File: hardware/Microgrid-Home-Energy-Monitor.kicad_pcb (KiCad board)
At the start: 2 copper layers, 41 parts, among them J1 AudioJack2, J2 AudioJack2, J3 Conn_01x04, J4 USB_C_Receptacle_USB2.0_16P, J5 Conn_01x06, J6 Conn_01x03, SW1 SW_Push, SW2 SW_Push, U1 ESP32-WROOM-32, U2 MCP6002-xP, U3 AMS1117-3.3

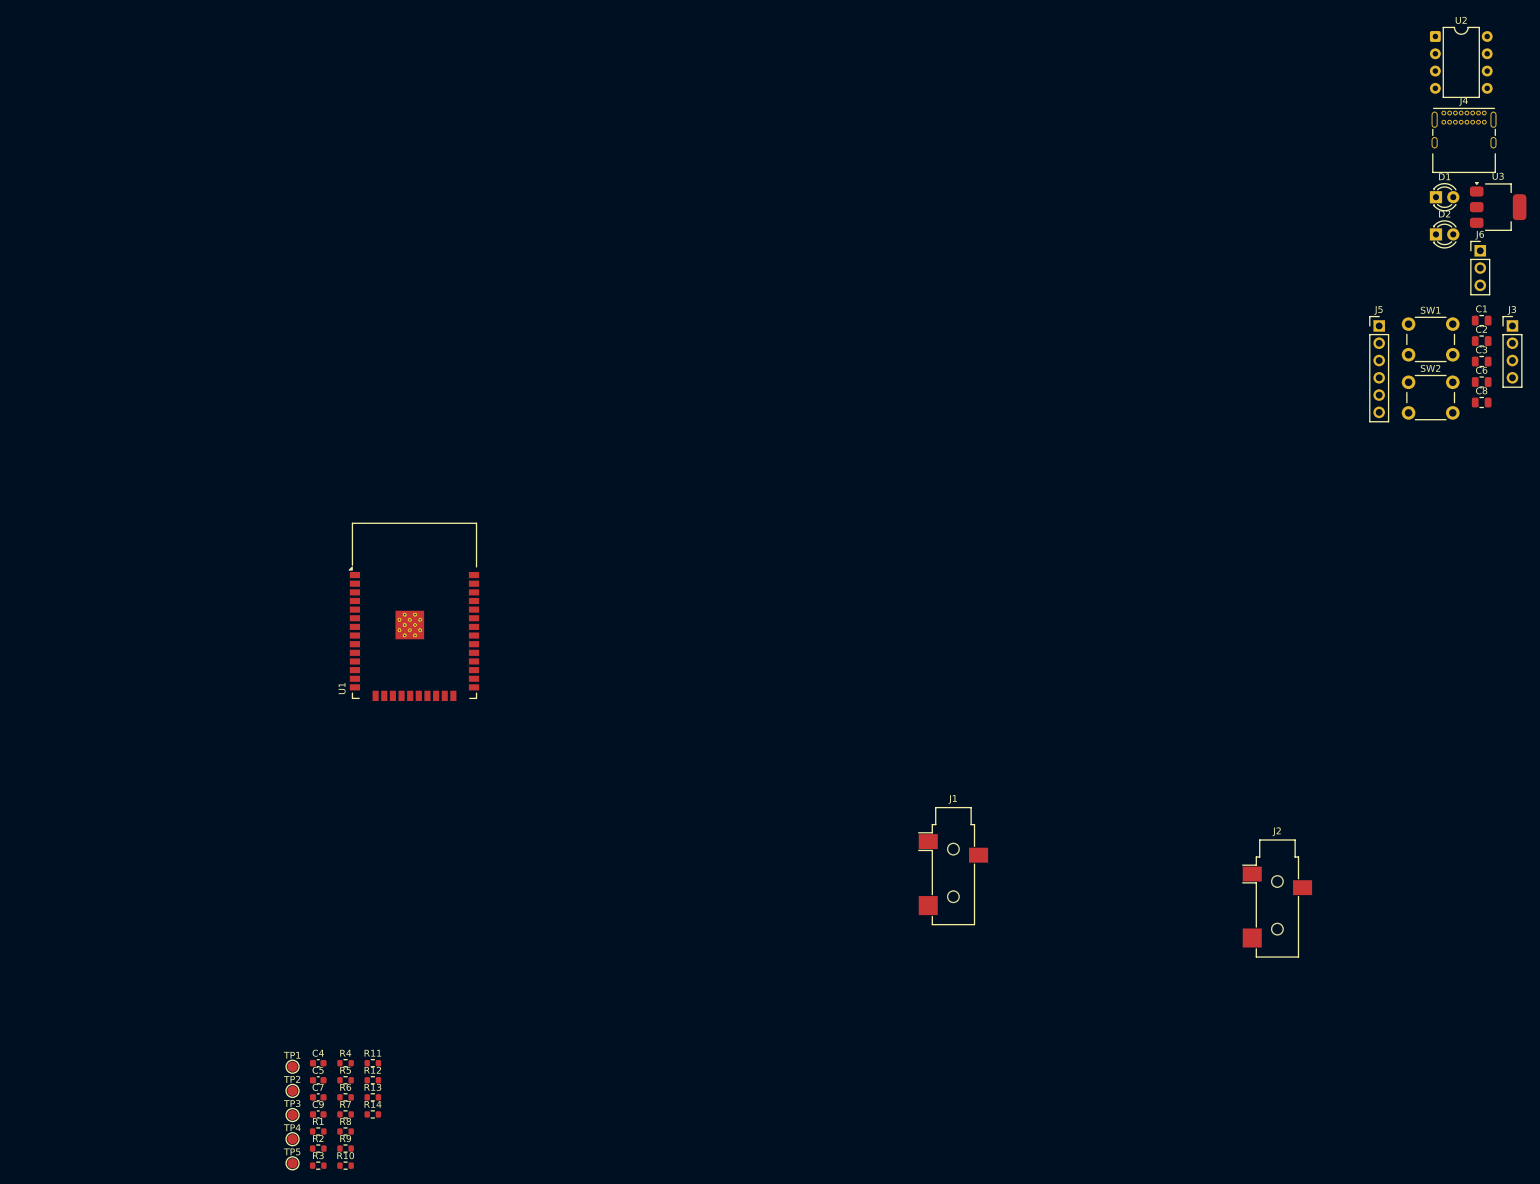
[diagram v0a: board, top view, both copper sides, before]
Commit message: Add Gerber fabrication files and update PCB with refilled copper pour
Gerbers generated from KiCad 9 for JLCPCB 2-layer fabrication.
Includes F.Cu, B.Cu, paste, mask, silkscreen, Edge.Cuts, and drill files.
PCB updated with refreshed GND zone fill before export.

Co-Authored-By: Claude Sonnet 4.6 <noreply@anthropic.com>
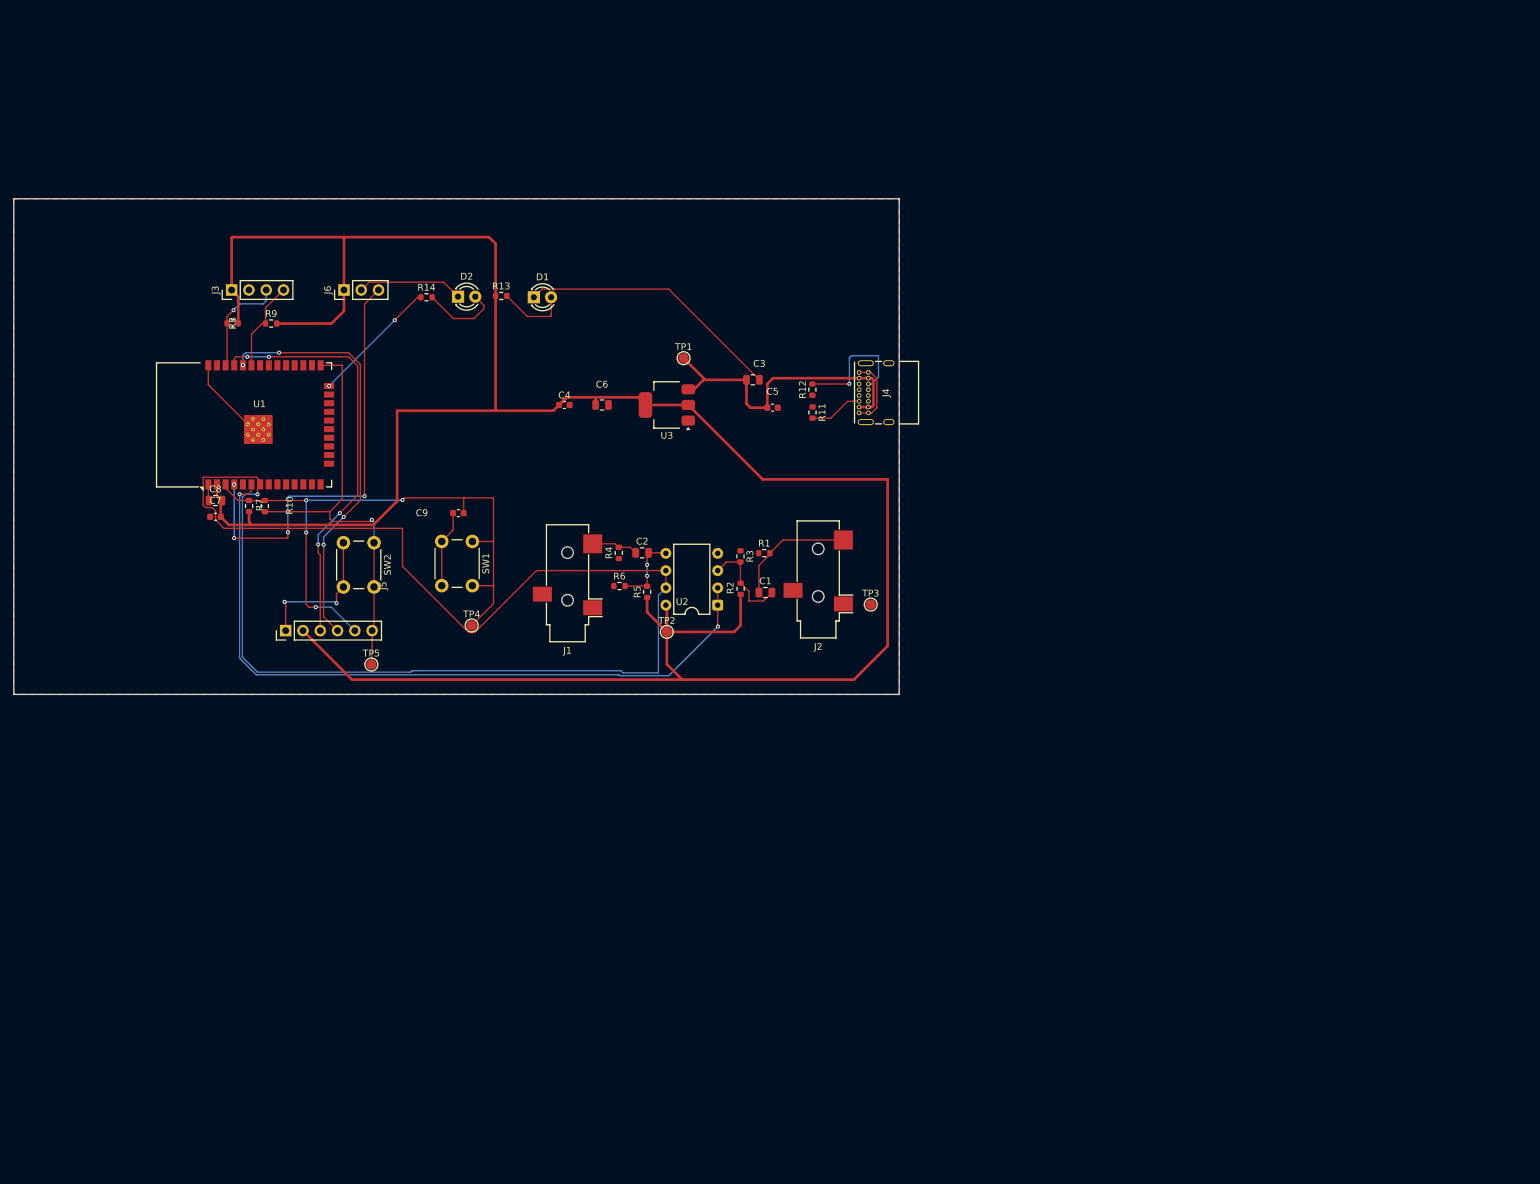
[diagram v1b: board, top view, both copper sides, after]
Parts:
- moved J3 188.3 mm to (90.5, 59.5), turned to 90 degrees
- moved C8 186.7 mm to (88.1, 90.5)
- moved J6 167.1 mm to (107.0, 59.5), turned to 90 degrees
- moved J5 166.9 mm to (98.4, 109.6), turned to 90 degrees
- moved SW2 153.9 mm to (111.4, 96.7), turned to -90 degrees
- moved D2 144.0 mm to (123.8, 60.5)
- moved SW1 141.3 mm to (125.9, 96.5), turned to -90 degrees
- moved U2 134.6 mm to (161.9, 105.9), turned to 180 degrees
- moved D1 133.4 mm to (134.9, 60.6)
- moved C6 129.3 mm to (144.9, 76.4)
- moved C2 127.3 mm to (150.8, 98.2)
- moved U3 125.6 mm to (154.5, 76.4), turned to 180 degrees
- moved R9 121.8 mm to (96.3, 64.5)
- moved R14 120.4 mm to (119.1, 60.6)
- moved R12 120.3 mm to (175.8, 74.2), turned to 90 degrees
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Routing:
- net +3.3V: track 0.00 -> 376.8 mm
- net /ADC_CH2: track 0.00 -> 202.1 mm, vias 0 -> 1
- net GND: track 0.00 -> 123.0 mm, vias 0 -> 2
- net /ADC_CH1: track 0.00 -> 107.1 mm, vias 0 -> 2
- net /EN: track 0.00 -> 93.5 mm, vias 0 -> 4
- net /VOLT_ADC: track 0.00 -> 64.3 mm, vias 0 -> 4
- net /IO0: track 0.00 -> 64.0 mm, vias 0 -> 1
- net /RX0: track 0.00 -> 61.8 mm, vias 0 -> 4
- net /TX0: track 0.00 -> 61.2 mm, vias 0 -> 4
- net VBUS: track 0.00 -> 45.8 mm
- net Net-(U1-IO2): track 0.00 -> 18.9 mm, vias 0 -> 2
- net Net-(J4-CC2): track 0.00 -> 18.7 mm, vias 0 -> 1
- net Net-(C1-Pad1): track 0.00 -> 18.1 mm
- net /SCL: track 0.00 -> 15.6 mm, vias 0 -> 1
- net Net-(U2A-+): track 0.00 -> 14.0 mm
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- added copper zone on F.Cu, net GND
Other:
- board outline added: 130.2 x 72.9 mm

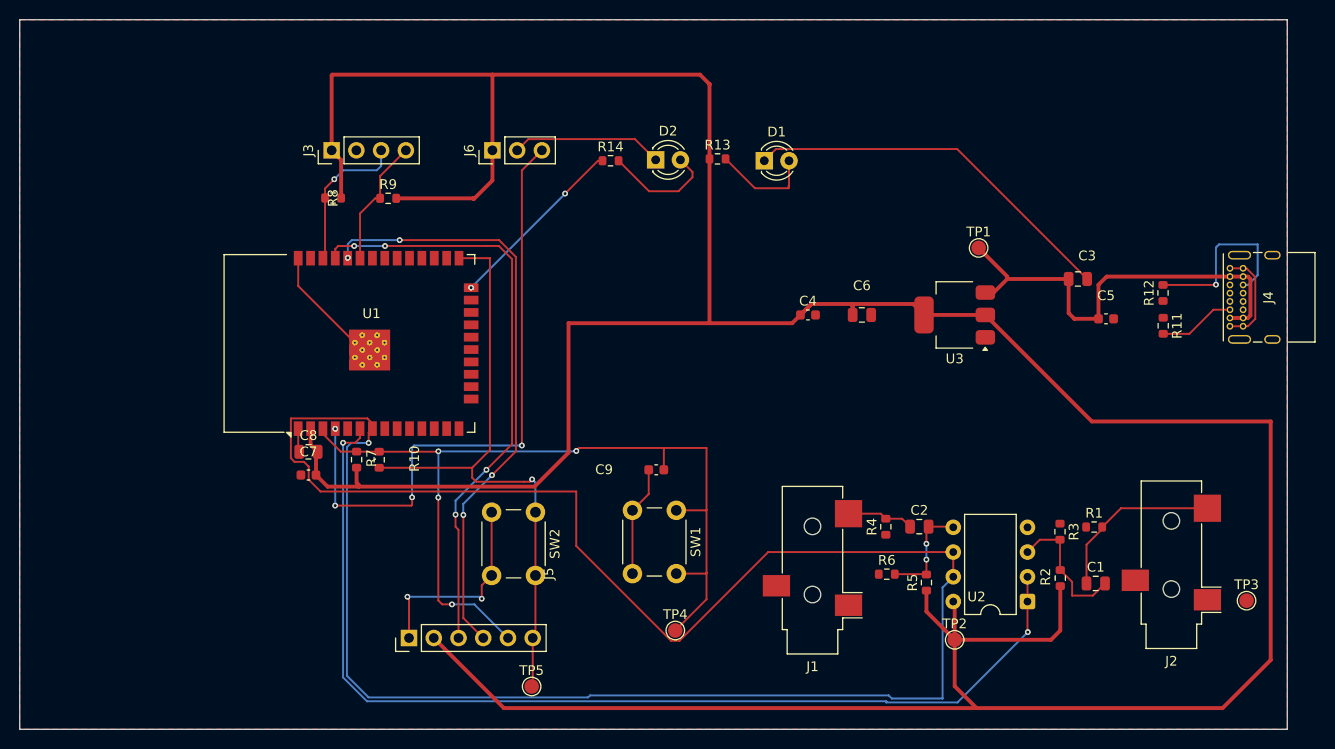
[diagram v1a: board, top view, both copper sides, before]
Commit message: Fix all DRC errors; sync fixed board + fresh Gerbers into repo
Board fixes (done in KiCad GUI):
- Added solid GND plane on B.Cu; stitching vias tie front pour fragments
  to it -- eliminates the split-pour GND islands permanently
- ESP32 thermal vias: 0.2mm -> 0.3mm drill (JLCPCB 2-layer minimum)
- Min clearance relaxed to fit the USB-C (J4) footprint's 0.15mm pad gaps

Verified with kicad-cli: DRC 0 violations, 0 unconnected. ERC 0 errors.
Gerbers + drill files re-exported from the fixed board -- ready for JLCPCB.

Note: the repo previously carried a stale June 14 copy of the board; the
edited project lived outside the repo. This commit syncs the real files.

Co-Authored-By: Claude Fable 5 <noreply@anthropic.com>
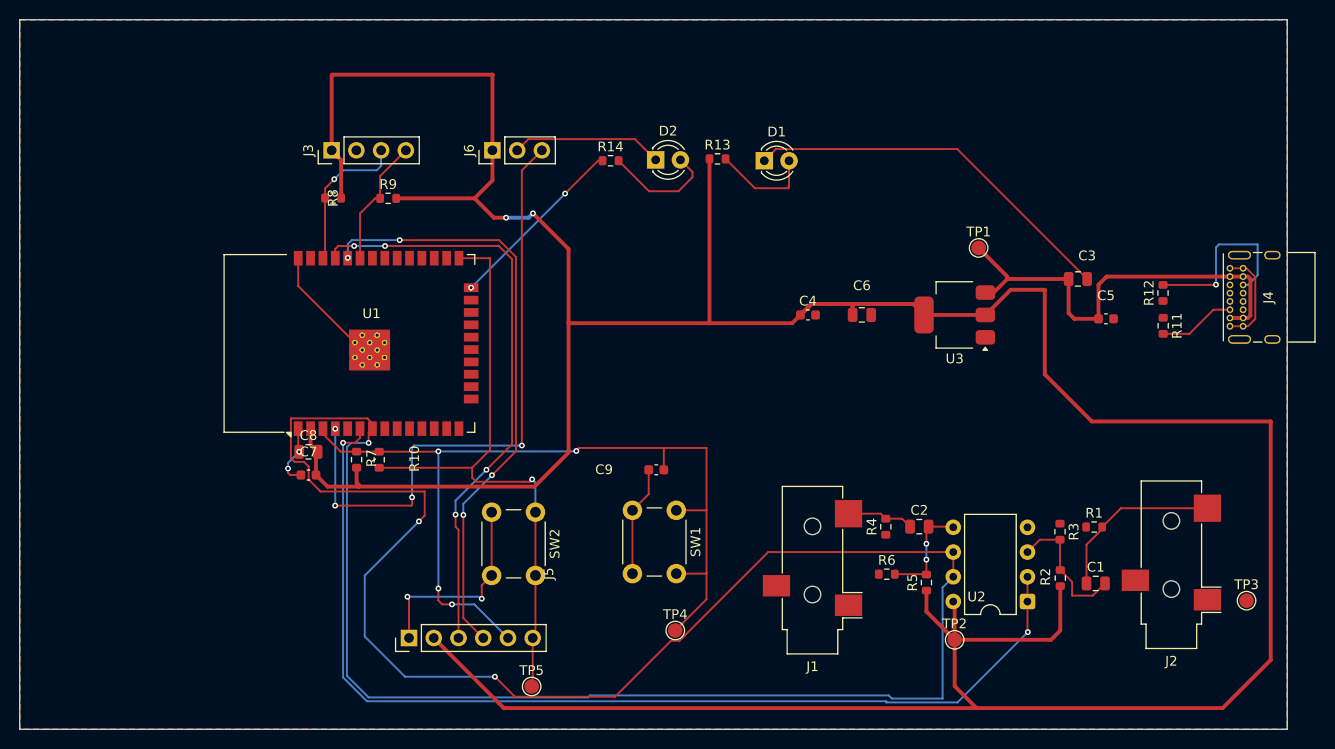
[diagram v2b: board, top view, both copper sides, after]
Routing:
- net /ADC_CH2: track 202.1 -> 221.0 mm, vias 1 -> 3
- net GND: track 123.0 -> 127.0 mm, vias 2 -> 4
- net +3.3V: track 376.8 -> 373.4 mm, vias 0 -> 2
- added copper zone on B.Cu, net GND
